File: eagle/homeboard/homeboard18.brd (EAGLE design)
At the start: 76.5 x 80.5 mm, 131 parts, among them IC1 XCF02S, IC2 25LC080SN, IC3 ATMEGA32U2-TQFP, Q5 BC848SMD, Q6 BC848SMD, Q7 BC848SMD, Q8 BC848SMD, T1 BSS138, T2 BC848, T3 BSS138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

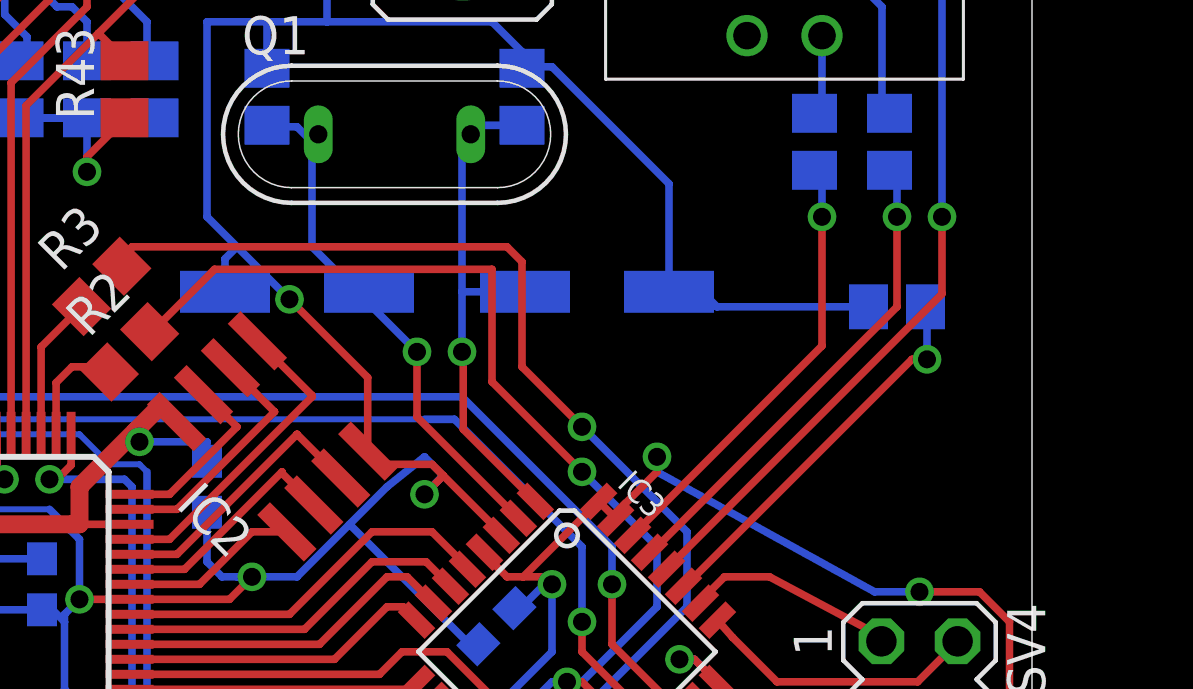
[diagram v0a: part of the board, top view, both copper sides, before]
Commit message: pull at_reset high
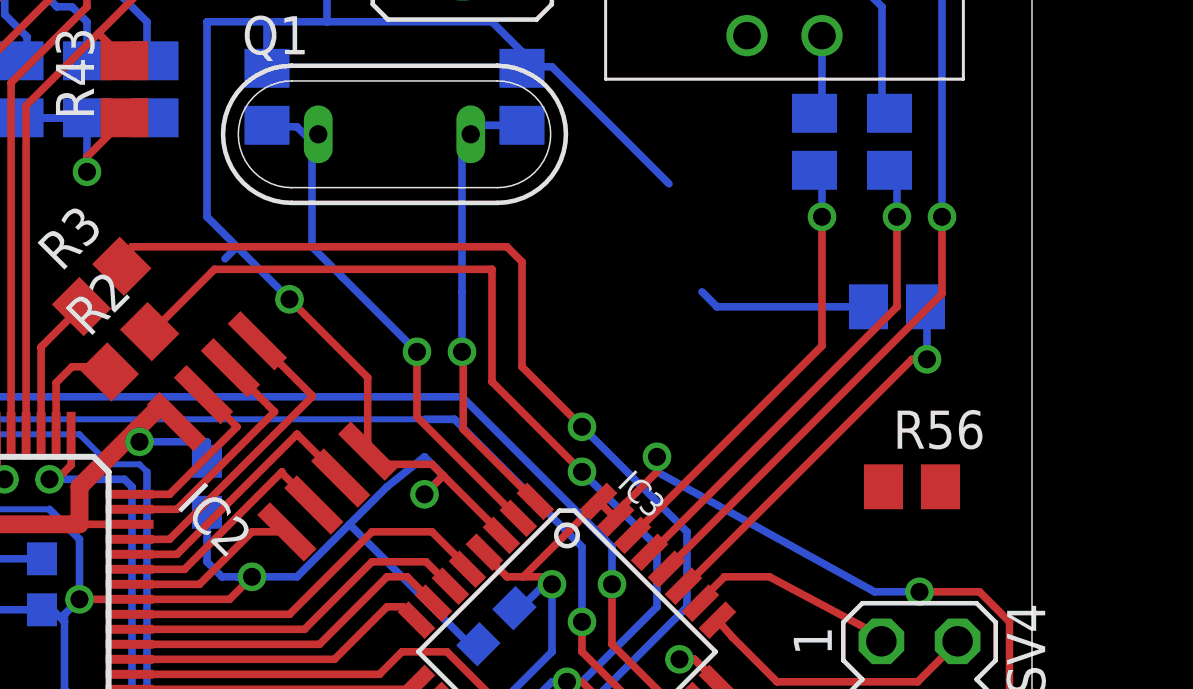
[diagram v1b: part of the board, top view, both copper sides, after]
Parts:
- removed C39, C40: 100u, rcl:PANASONIC_D
- added R56: 4700, rcl:R0805
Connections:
- net AT_RESET: now also R56.2
- net GND: no longer C39.-, C40.-
- net N$12: no longer C40.+
- net N$14: no longer C39.+
- net VCC: now also R56.1
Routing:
- net GND: track 824.3 -> 818.5 mm
- net N$14: track 17.3 -> 15.2 mm
- net N$12: track 18.5 -> 17.5 mm
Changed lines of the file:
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@@
 <layer number="42" name="bRestrict" color="1" fill="10" visible="yes" active="yes"/>
 <layer number="43" name="vRestrict" color="2" fill="10" visible="yes" active="yes"/>
-<layer number="44" name="Drills" color="7" fill="1" visible="no" active="yes"/>
-<layer number="45" name="Holes" color="7" fill="1" visible="no" active="yes"/>
+<layer number="44" name="Drills" color="7" fill="1" visible="yes" active="yes"/>
+<layer number="45" name="Holes" color="7" fill="1" visible="yes" active="yes"/>
 <layer number="46" name="Milling" color="3" fill="1" visible="no" active="yes"/>
 <layer number="47" name="Measures" color="7" fill="1" visible="no" active="yes"/>
@@
 <element name="C37" library="rcl" package="C0805" value="" x="51" y="63" rot="MR270"/>
 <element name="C38" library="rcl" package="C0805" value="" x="59.5" y="63" rot="MR270"/>
-<element name="C39" library="rcl" package="PANASONIC_D" value="100u" x="62" y="56.5" rot="MR0"/>
-<element name="C40" library="rcl" package="PANASONIC_D" value="100u" x="52" y="56.5" rot="MR180"/>
 <element name="PWR_HDR" library="jumper" package="JP1" value="" x="17.3" y="12.34" rot="R90"/>
 <element name="X8" library="cpcfpga" package="20-0137" value="STEREOJACK" x="23" y="71.5" rot="R270"/>
@@
 <attribute name="OC_FARNELL" value="unknown" x="62.96966875" y="34.573225" size="1.778" layer="27" rot="R315" display="off"/>
 </element>
+<element name="R56" library="rcl" package="R0805" value="4700" x="72.5" y="50"/>
 </elements>
 <signals>
@@
 <wire x1="15.11" y1="56.89" x2="15.5" y2="56.5" width="0.254" layer="16"/>
 <contactref element="C38" pad="1"/>
-<contactref element="C39" pad="-"/>
-<contactref element="C40" pad="-"/>
 <contactref element="C37" pad="1"/>
 <contactref element="PWR_HDR" pad="1"/>
@@
 <wire x1="59.5" y1="64.5" x2="58.5" y2="65.5" width="0.254" layer="16"/>
 <wire x1="51" y1="65.5" x2="51" y2="63.95" width="0.254" layer="16"/>
-<wire x1="49.6" y1="56.5" x2="49.6" y2="57.6" width="0.254" layer="16"/>
 <wire x1="49.6" y1="57.6" x2="50" y2="58" width="0.254" layer="16"/>
-<wire x1="64.4" y1="56.5" x2="64.4" y2="60.1" width="0.254" layer="16"/>
 <wire x1="64.4" y1="60.1" x2="60.5" y2="64" width="0.254" layer="16"/>
 <wire x1="60.5" y1="64" x2="59.55" y2="64" width="0.254" layer="16"/>
 <wire x1="59.55" y1="64" x2="59.5" y2="63.95" width="0.254" layer="16"/>
 <contactref element="C41" pad="2"/>
-<wire x1="65.5" y1="56.5" x2="64.4" y2="56.5" width="0.254" layer="16"/>
 <wire x1="75.52" y1="37.23" x2="75.75" y2="36.5" width="0.254" layer="16"/>
 <wire x1="75.75" y1="36.5" x2="75.75" y2="31.25" width="0.254" layer="16"/>
@@
 <wire x1="83.23" y1="64.93" x2="94.77" y2="63.1284" width="0" layer="19" extent="1-1"/>
 <wire x1="71.05" y1="56" x2="83.23" y2="64.93" width="0" layer="19" extent="16-16"/>
+<wire x1="64.4" y1="60.1" x2="65.5" y2="56.5" width="0" layer="19" extent="16-16"/>
 <wire x1="41.97" y1="51.7" x2="42" y2="51.75" width="0" layer="19" extent="1-1"/>
 <wire x1="29.47" y1="51.7" x2="29.5" y2="51.75" width="0" layer="19" extent="1-1"/>
@@
 <wire x1="75.75" y1="34.45" x2="75.75" y2="30.55" width="0.254" layer="1"/>
 <wire x1="75.75" y1="30.55" x2="74.95" y2="29.75" width="0.254" layer="1"/>
+<contactref element="R56" pad="1"/>
 <wire x1="74.75" y1="46.5" x2="85.77" y2="64.93" width="0" layer="19" extent="1-1"/>
 <wire x1="74.02" y1="34.69" x2="74" y2="34.75" width="0" layer="19" extent="1-1"/>
@@
 <wire x1="93.95" y1="25.5" x2="88" y2="25.4" width="0" layer="19" extent="1-1"/>
 <wire x1="91" y1="42.1" x2="86.65" y2="35.5" width="0" layer="19" extent="1-1"/>
+<wire x1="71.55" y1="50" x2="13.5" y2="21.5" width="0" layer="19" extent="1-1"/>
 </signal>
 <signal name="TCK">
@@
 <signal name="N$12">
 <contactref element="C37" pad="2"/>
-<contactref element="C40" pad="+"/>
 <contactref element="Q1" pad="1"/>
 <contactref element="IC3" pad="2"/>
@@
 <wire x1="52.5" y1="61.5" x2="52.5" y2="61.54" width="0.254" layer="16"/>
 <wire x1="51" y1="62.05" x2="51" y2="62" width="0.254" layer="16"/>
-<wire x1="54.4" y1="56.5" x2="53.5" y2="57" width="0.254" layer="16"/>
 <wire x1="52.5" y1="61.54" x2="52.71" y2="61.75" width="0.254" layer="16"/>
 <wire x1="51" y1="62" x2="52" y2="62" width="0.254" layer="16"/>
@@
 <signal name="N$14">
 <contactref element="Q1" pad="2"/>
-<contactref element="C39" pad="+"/>
 <contactref element="C38" pad="2"/>
 <contactref element="IC3" pad="1"/>
@@
 <wire x1="57.5" y1="54.5" x2="57.5" y2="56.5" width="0.254" layer="16"/>
 <wire x1="57.5" y1="56.5" x2="57.5" y2="61.5" width="0.254" layer="16"/>
-<wire x1="59.6" y1="56.5" x2="57.5" y2="56.5" width="0.254" layer="16"/>
 <wire x1="57.5" y1="61.5" x2="57.75" y2="61.75" width="0.254" layer="16"/>
 <wire x1="59.5" y1="62.05" x2="58.09" y2="62.05" width="0.254" layer="16"/>
@@
 <wire x1="74.02" y1="39.77" x2="74.02" y2="40.48" width="0.254" layer="16"/>
 <wire x1="74.02" y1="40.48" x2="74" y2="40.5" width="0.254" layer="16"/>
+<contactref element="R56" pad="2"/>
+<wire x1="73.45" y1="50" x2="66.5" y2="41" width="0" layer="19" extent="1-16"/>
 </signal>
 <signal name="PC4">

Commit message: mah
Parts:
- added U$1: SDMMCSCDA, adafruit:SCDA
- moved R56 1.00 mm to (72.5, 51.0)
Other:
- board size 76.5 x 80.5 mm -> 76.5 x 80 mm
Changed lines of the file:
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@@
 <board>
 <plain>
-<wire x1="0" y1="0" x2="76.5" y2="-0.5" width="0" layer="20"/>
-<wire x1="76.5" y1="-0.5" x2="76.5" y2="79.5" width="0" layer="20"/>
-<wire x1="76.5" y1="79.5" x2="0" y2="80" width="0" layer="20"/>
+<wire x1="0" y1="0" x2="76.5" y2="0" width="0" layer="20"/>
+<wire x1="76.5" y1="0" x2="76.5" y2="80" width="0" layer="20"/>
+<wire x1="76.5" y1="80" x2="0" y2="80" width="0" layer="20"/>
 <wire x1="0" y1="80" x2="0" y2="0" width="0" layer="20"/>
 </plain>
@@
 <attribute name="OC_FARNELL" value="unknown" x="62.96966875" y="34.573225" size="1.778" layer="27" rot="R315" display="off"/>
 </element>
-<element name="R56" library="rcl" package="R0805" value="4700" x="72.5" y="50"/>
+<element name="R56" library="rcl" package="R0805" value="4700" x="72.5" y="51"/>
+<element name="U$1" library="adafruit" package="SCDA" value="SDMMCSCDA" x="-21" y="19.5"/>
 </elements>
 <signals>
@@
 <wire x1="93.95" y1="25.5" x2="88" y2="25.4" width="0" layer="19" extent="1-1"/>
 <wire x1="91" y1="42.1" x2="86.65" y2="35.5" width="0" layer="19" extent="1-1"/>
-<wire x1="71.55" y1="50" x2="13.5" y2="21.5" width="0" layer="19" extent="1-1"/>
+<wire x1="71.55" y1="51" x2="13.5" y2="21.5" width="0" layer="19" extent="1-1"/>
 </signal>
 <signal name="TCK">
@@
 <wire x1="74.02" y1="40.48" x2="74" y2="40.5" width="0.254" layer="16"/>
 <contactref element="R56" pad="2"/>
-<wire x1="73.45" y1="50" x2="66.5" y2="41" width="0" layer="19" extent="1-16"/>
+<wire x1="73.45" y1="51" x2="66.5" y2="41" width="0" layer="19" extent="1-16"/>
 </signal>
 <signal name="PC4">

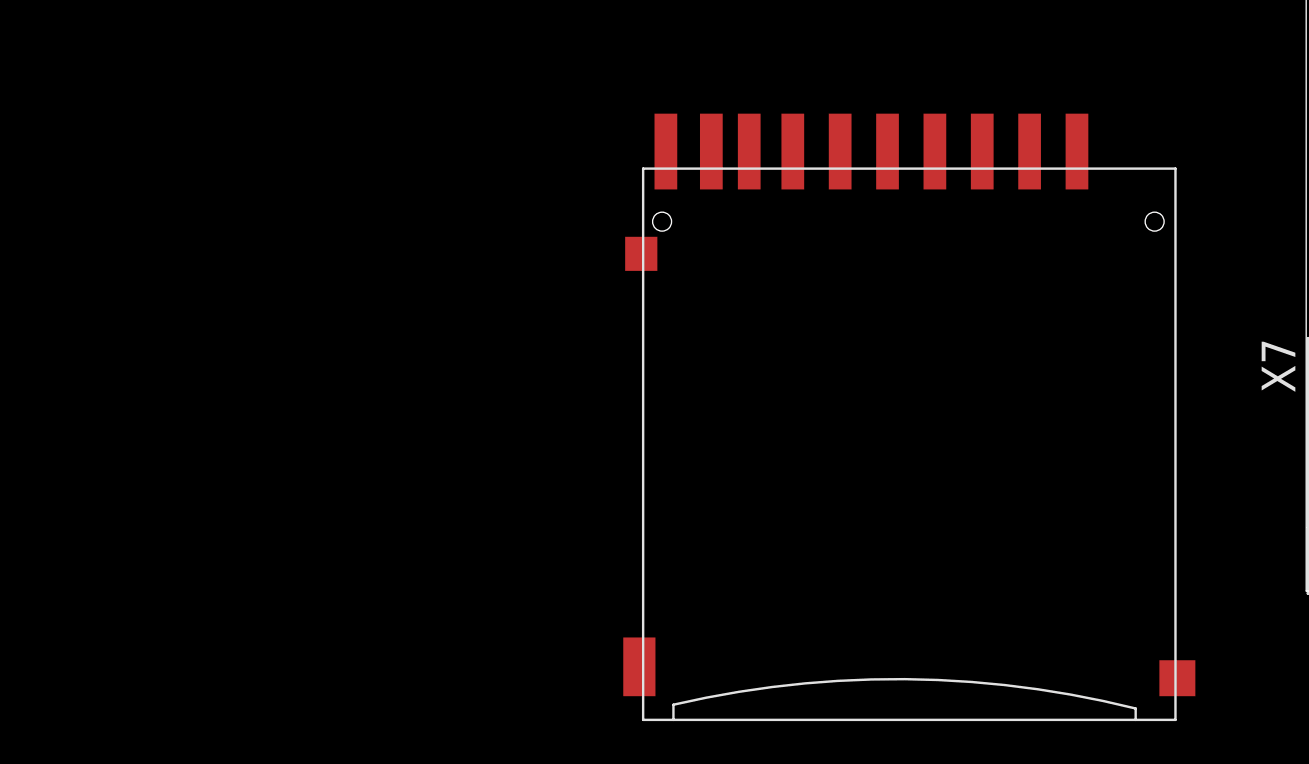
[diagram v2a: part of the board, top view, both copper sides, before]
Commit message: sd/mmc connector to match the nohole ones i have - to mount underneatj board
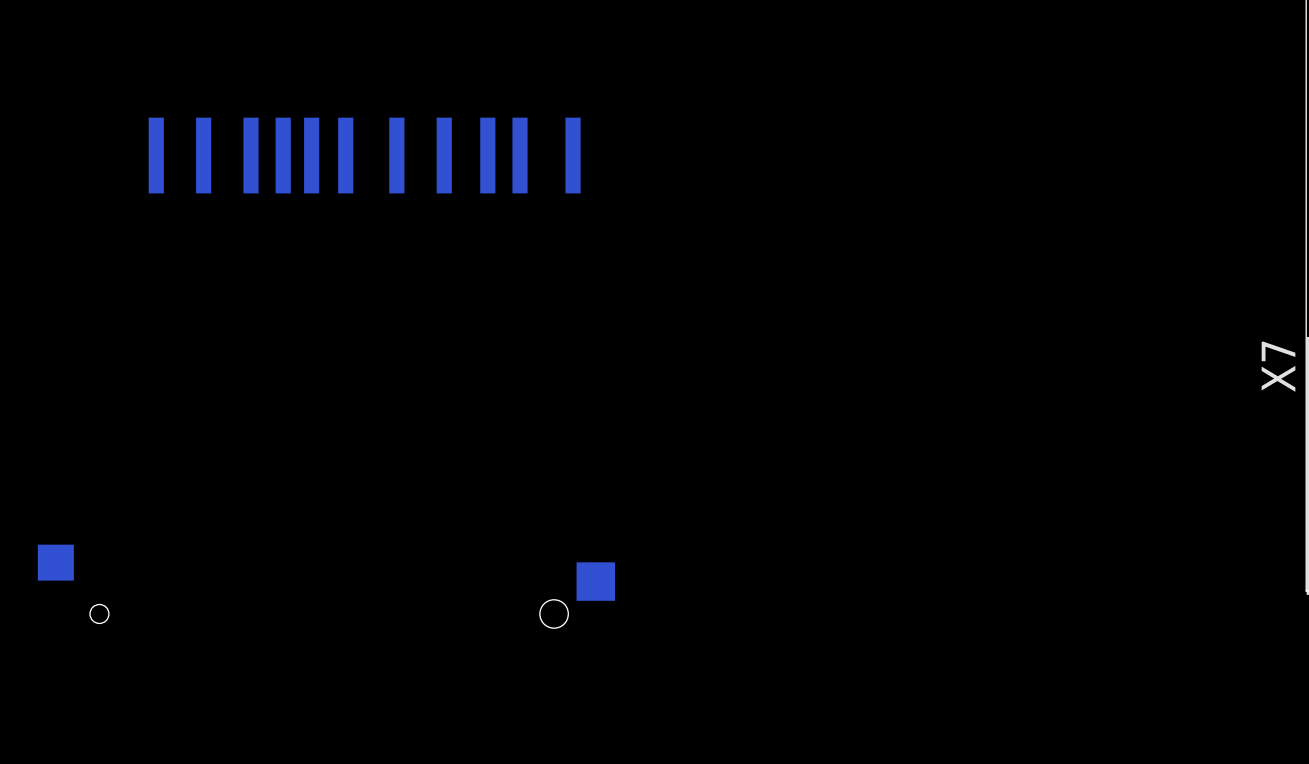
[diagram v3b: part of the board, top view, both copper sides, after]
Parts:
- removed U$1: SDMMCSCDA, adafruit:SCDA
- added U$3: SDMMCNOHOLE, cpcfpga:SDCARD-NOHOLE
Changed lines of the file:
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@@
 </element>
 <element name="R56" library="rcl" package="R0805" value="4700" x="72.5" y="51"/>
-<element name="U$1" library="adafruit" package="SCDA" value="SDMMCSCDA" x="-21" y="19.5"/>
+<element name="U$3" library="cpcfpga" package="SDCARD-NOHOLE" value="SDMMCNOHOLE" x="-66" y="22"/>
 </elements>
 <signals>

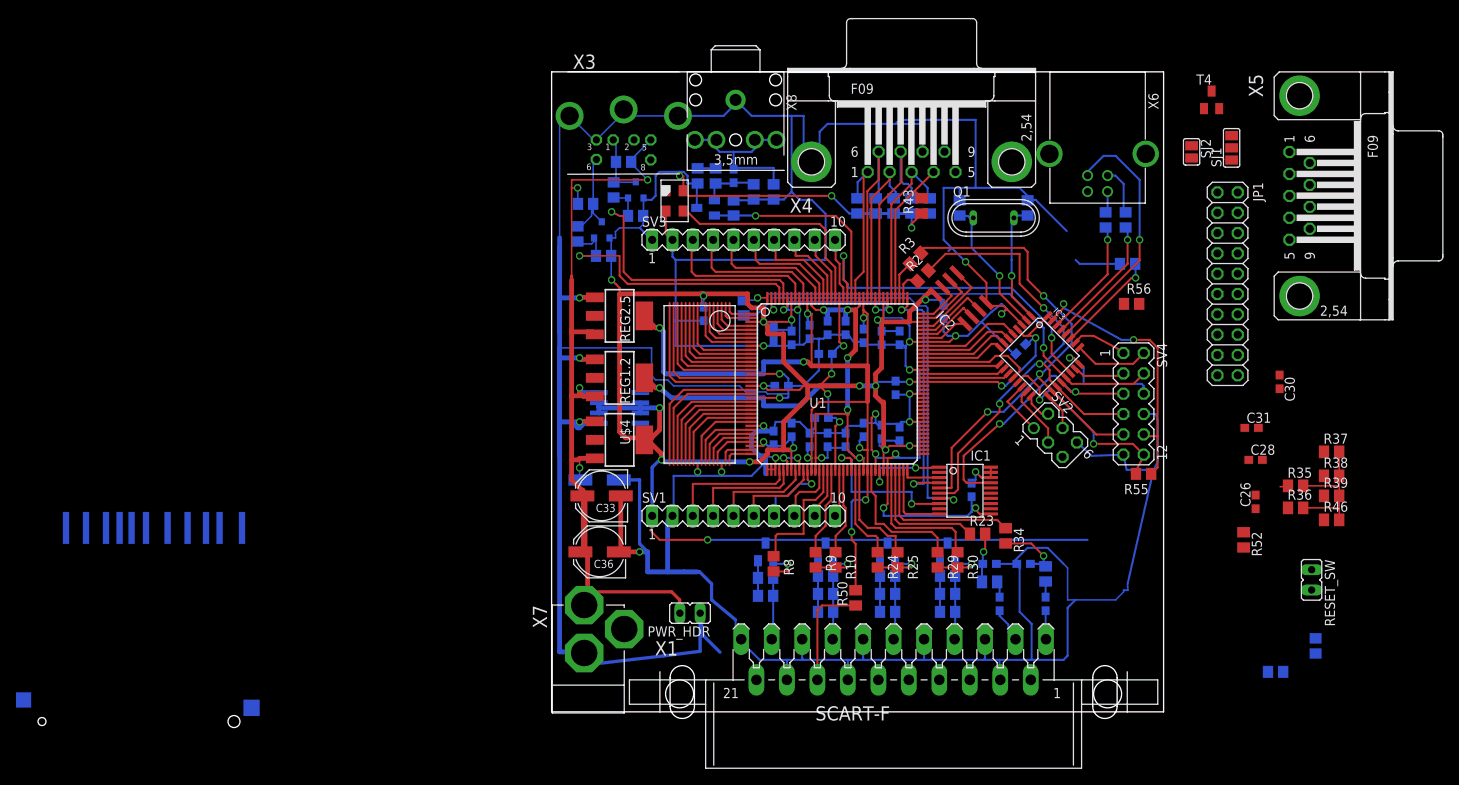
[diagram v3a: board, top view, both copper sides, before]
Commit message: added sd/mmc connector and made a bit of a mess
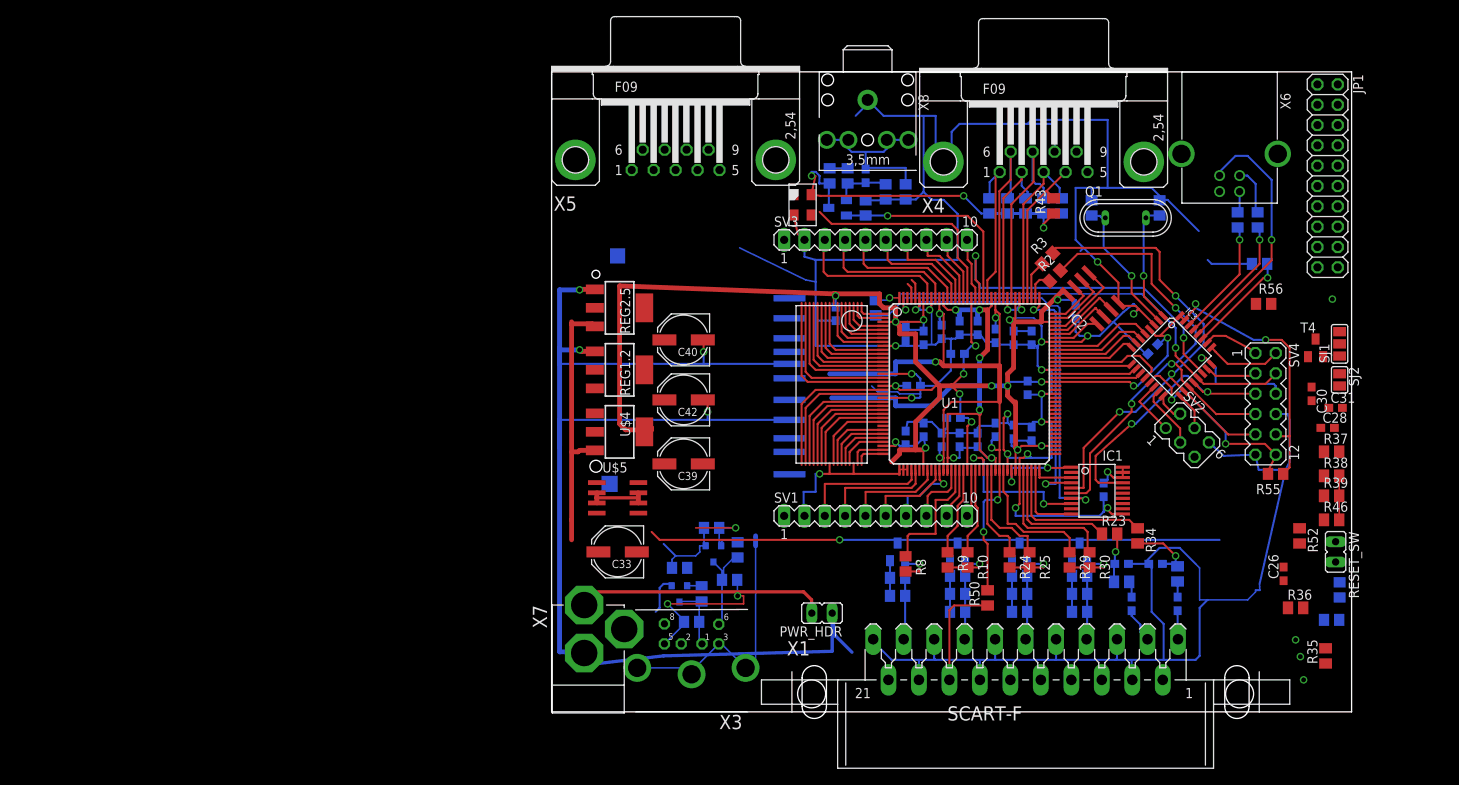
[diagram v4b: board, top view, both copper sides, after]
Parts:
- removed C35, C36: 100u, rcl:PANASONIC_D
- added C39, C40, C42: 100u, rcl:PANASONIC_D
- moved U$3 101.0 mm to (28.8, 57.0), turned to 270 degrees
- moved X5 78.1 mm to (15.5, 69.0), turned to 0 degrees
- moved X3 71.0 mm to (17.5, 4.75), turned to 180 degrees
- moved R7 58.1 mm to (17.5, 11.2), turned to 0 degrees
- moved R51 51.7 mm to (18.8, 14.8), turned to 90 degrees
- moved T3 50.8 mm to (16.0, 14.8), turned to 0 degrees
- moved R5 50.3 mm to (22.2, 16.5), turned to 180 degrees
- moved R6 44.3 mm to (16.0, 18.0), turned to 0 degrees
- moved R47 44.3 mm to (23.2, 20.2), turned to 90 degrees
- moved T1 42.9 mm to (20.2, 19.8), turned to 0 degrees
- moved R4 36.6 mm to (20.0, 23.0), turned to 0 degrees
- moved SJ2 34.0 mm to (98.5, 41.5)
- moved T4 33.6 mm to (95.5, 45.5)
- moved SJ1 28.0 mm to (98.5, 46.0)
- moved R35 21.6 mm to (96.8, 7.00), turned to 90 degrees
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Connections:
- new net SD_CLK: U$3.5
- new net SD_CS: U$3.1
- new net SD_DI: U$3.2
- new net SD_DO: U$3.7
- net GND: now also C39.-, C40.-, C42.-, U$3.3, U$3.6, U$3.MT1, U$3.MT3; no longer C35.-, C36.-
- net VCC: now also C39.+, U$3.4
- net VCC5: no longer C35.+, C36.+
- net VCCAUX: now also C40.+
- net VCCINT: now also C42.+
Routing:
- net GND: track 818.5 -> 756.1 mm, vias 29 -> 26
- net PS2DAT: track 37.3 -> 4.33 mm, vias 1 -> 0
- net PS2CLK: track 36.5 -> 14.1 mm
- net VCC: track 464.7 -> 442.3 mm, vias 30 -> 26
- net VCC5: track 104.5 -> 84.5 mm
- net VCCAUX: track 110.4 -> 96.1 mm, vias 8 -> 7
- net VCCINT: track 83.1 -> 75.0 mm, vias 7 -> 6
- net JOY1_FIRE1: track 1.01 -> 0.00 mm
- net JOY1_FIRE2: track 0.51 -> 0.00 mm
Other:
- board size 76.5 x 80 mm -> 100 x 80 mm
